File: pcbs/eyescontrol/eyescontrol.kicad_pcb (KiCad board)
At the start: 2 copper layers, 40.6 x 43.2 mm, 15 parts, among them IC1 ATMEGA88-P, P1 EYES, P2 PROG_MICRO, P3 CONN_01X04, SW1 SW_PUSH, Y1 18.432 MHz

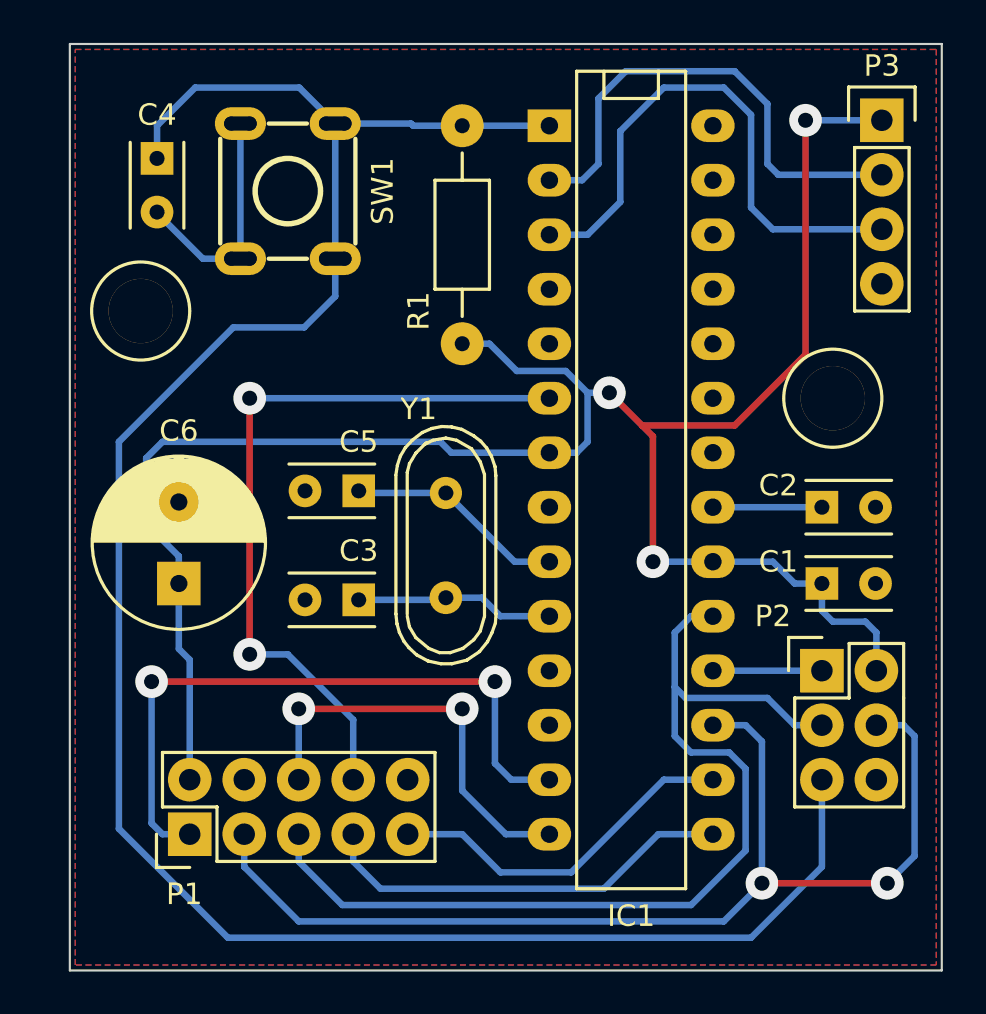
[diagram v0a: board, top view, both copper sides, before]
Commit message: actualizo las 3 placas, revisar y mandar a fabricar
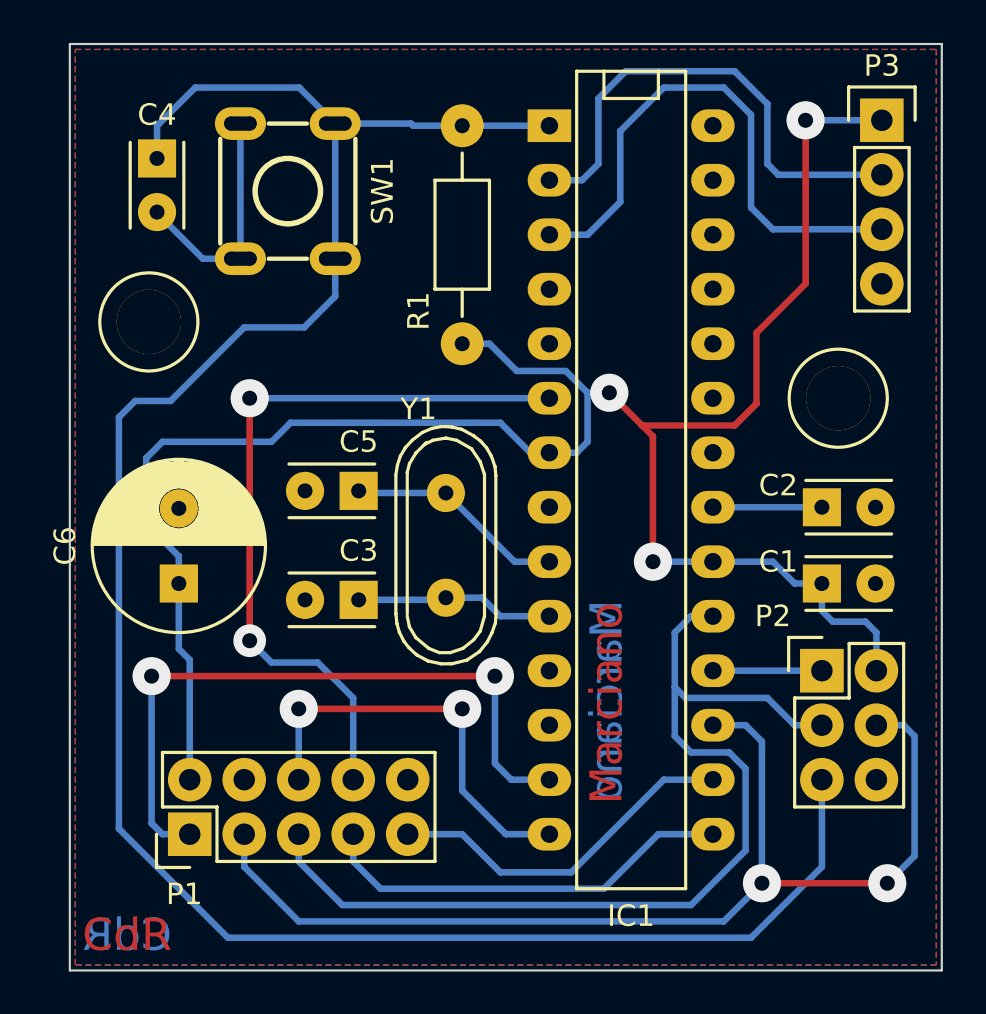
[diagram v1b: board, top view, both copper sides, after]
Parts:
- C3, C5: value 22n -> 15p
- C6: value 33m -> 330u; footprint Capacitors_ThroughHole:C_Radial_D8_L13_P3.8 -> Capacitors_ThroughHole:C_Radial_D8_L11.5_P3.5
- moved REF** 0.63 mm to (93.3, 96.5)
- moved REF** 0.25 mm to (125.5, 100.1)
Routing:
- net +5V: track 93.7 -> 94.5 mm
- net /RST: track 100.1 -> 100.8 mm
- net /VPRG: track 31.3 -> 31.8 mm
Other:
- net class Default: via_dia 1.524 -> 1.778
- board text added: "CdR"
- board text added: "Marciano"

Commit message: cambios hechos en las placas
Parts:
- added REF**: 1pin, Connect:1pin, F.Cu at (104.1, 97.0)
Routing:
- net /MOSI: track 51.9 -> 52.4 mm
